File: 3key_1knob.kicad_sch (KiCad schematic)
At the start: 17 parts, among them SW1 RotaryEncoder_Switch, U4 Kailh_socket_MX, U5 Kailh_socket_MX, U6 Kailh_socket_MX

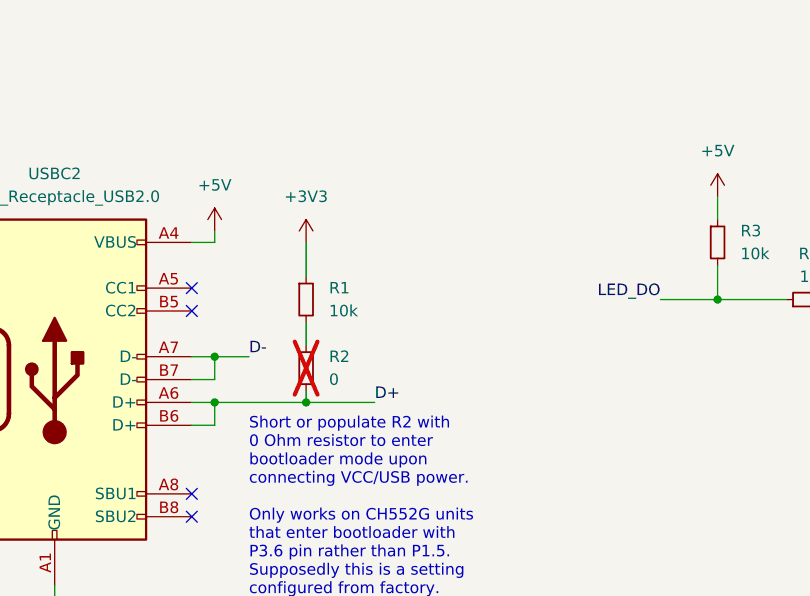
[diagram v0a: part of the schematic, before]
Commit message: Finish ground fills; Add 2 pin header; Update 3D models
This completes the PCB drawing based off the (questionable) original
design. Due to odd signal routing, there are several ground fill islands
that had to be addressed by placing microvias.

Note that with JLCPCB DRC constraints, there will be some spacing
violations due to the USBC footprint used. The USBC footprint has 2
mounting holes which are too close to power pads.

This also hides R2 resistor 3D model and displays 16-SOIC-3.9x9.9mm 3D
model. For reference, R2 is unconnected, and 16-SOP-3.9x9.9mm lacks a 3D
model so I used 16-SOIC variant instead.
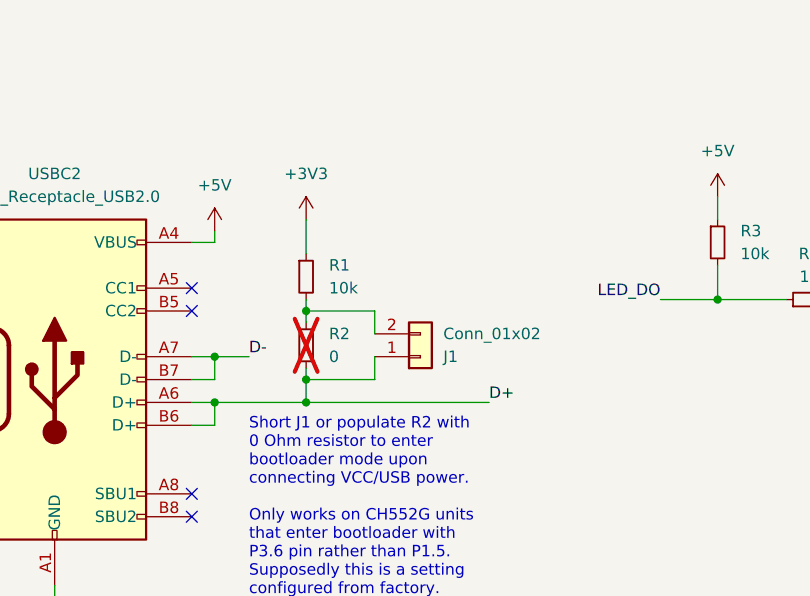
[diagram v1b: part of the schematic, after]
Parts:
- added J1: Conn_01x02, Connector_PinHeader_1.27mm:PinHeader_1x02_P1.27mm_Vertical, symbol Connector_Generic:Conn_01x02
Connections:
- net D+: now also J1.1 (Pin_1)
- net at R1.2, R2.1: now also J1.2 (Pin_2)
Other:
- note added: "Short J1 or populate R2 with 0 Ohm resistor to enter bootloader mode upon connecting VCC/USB power. Only works on CH552G units that enter bootloader with P3.6 pin rather than P1.5. Supposedly this is a setting configured from factory."
- note removed: "Short or populate R2 with 0 Ohm resistor to enter bootloader mode upon connecting VCC/USB power. Only works on CH552G units that enter bootloader with P3.6 pin rather than P1.5. Supposedly this is a setting configured from factory."
- moved on the sheet: R1, R2
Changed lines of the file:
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@@
   (junction (at 105.41 71.12) (diameter 0) (color 0 0 0 0)
+  )
+  (junction (at 59.69 80.01) (diameter 0) (color 0 0 0 0)
+  )
+  (junction (at 59.69 72.39) (diameter 0) (color 0 0 0 0)
   )
   (junction (at 49.53 82.55) (diameter 0) (color 0 0 0 0)
@@
     (stroke (width 0) (type default))
   )
+  (wire (pts (xy 59.69 80.01) (xy 59.69 82.55))
+    (stroke (width 0) (type default))
+  )
   (wire (pts (xy 46.99 82.55) (xy 49.53 82.55))
     (stroke (width 0) (type default))
@@
     (stroke (width 0) (type default))
   )
+  (wire (pts (xy 67.31 72.39) (xy 59.69 72.39))
+    (stroke (width 0) (type default))
+  )
   (wire (pts (xy 127 39.37) (xy 124.46 39.37))
     (stroke (width 0) (type default))
@@
     (stroke (width 0) (type default))
   )
+  (wire (pts (xy 67.31 80.01) (xy 59.69 80.01))
+    (stroke (width 0) (type default))
+  )
   (wire (pts (xy 49.53 77.47) (xy 53.34 77.47))
     (stroke (width 0) (type default))
@@
     (stroke (width 0) (type default))
   )
-  (wire (pts (xy 59.69 81.28) (xy 59.69 82.55))
+  (wire (pts (xy 59.69 78.74) (xy 59.69 80.01))
     (stroke (width 0) (type default))
   )
@@
     (stroke (width 0) (type default))
   )
-  (wire (pts (xy 59.69 82.55) (xy 67.31 82.55))
+  (wire (pts (xy 59.69 82.55) (xy 80.01 82.55))
     (stroke (width 0) (type default))
   )
@@
     (stroke (width 0) (type default))
   )
+  (wire (pts (xy 59.69 72.39) (xy 59.69 73.66))
+    (stroke (width 0) (type default))
+  )
+  (wire (pts (xy 67.31 77.47) (xy 67.31 80.01))
+    (stroke (width 0) (type default))
+  )
   (wire (pts (xy 49.53 85.09) (xy 49.53 82.55))
     (stroke (width 0) (type default))
@@
     (stroke (width 0) (type default))
   )
-  (wire (pts (xy 59.69 73.66) (xy 59.69 76.2))
-    (stroke (width 0) (type default))
-  )
-  (wire (pts (xy 59.69 64.77) (xy 59.69 68.58))
+  (wire (pts (xy 59.69 71.12) (xy 59.69 72.39))
+    (stroke (width 0) (type default))
+  )
+  (wire (pts (xy 59.69 62.23) (xy 59.69 66.04))
     (stroke (width 0) (type default))
   )
@@
   )
   (wire (pts (xy 128.27 147.32) (xy 133.35 147.32))
+    (stroke (width 0) (type default))
+  )
+  (wire (pts (xy 67.31 74.93) (xy 67.31 72.39))
     (stroke (width 0) (type default))
   )
@@
     (effects (font (size 1.27 1.27)) (justify left bottom))
   )
-  (text "Short or populate R2 with\n0 Ohm resistor to enter\nbootloader mode upon\nconnecting VCC/USB power.\n\nOnly works on CH552G units\nthat enter bootloader with\nP3.6 pin rather than P1.5.\nSupposedly this is a setting\nconfigured from factory."
+  (text "Short J1 or populate R2 with\n0 Ohm resistor to enter\nbootloader mode upon\nconnecting VCC/USB power.\n\nOnly works on CH552G units\nthat enter bootloader with\nP3.6 pin rather than P1.5.\nSupposedly this is a setting\nconfigured from factory."
     (at 53.34 104.14 0)
     (effects (font (size 1.27 1.27)) (justify left bottom))
@@
     (effects (font (size 1.27 1.27)) (justify left bottom))
   )
-  (label "D+" (at 67.31 82.55 0) (fields_autoplaced)
+  (label "D+" (at 80.01 82.55 0) (fields_autoplaced)
     (effects (font (size 1.27 1.27)) (justify left bottom))
   )
@@
     )
   )
-  (symbol (lib_id "Device:R_Small") (at 59.69 71.12 0) (unit 1)
-    (in_bom yes) (on_board yes) (dnp no) (fields_autoplaced)
-    (property "Reference" "R1" (at 62.23 69.85 0)
-      (effects (font (size 1.27 1.27)) (justify left))
-    )
-    (property "Value" "10k" (at 62.23 72.39 0)
-      (effects (font (size 1.27 1.27)) (justify left))
-    )
-    (property "Footprint" "Resistor_SMD:R_0603_1608Metric" (at 59.69 71.12 0)
-      (effects (font (size 1.27 1.27)) hide)
-    )
-    (property "Datasheet" "~" (at 59.69 71.12 0)
+  (symbol (lib_id "Device:R_Small") (at 59.69 68.58 0) (unit 1)
+    (in_bom yes) (on_board yes) (dnp no) (fields_autoplaced)
+    (property "Reference" "R1" (at 62.23 67.31 0)
+      (effects (font (size 1.27 1.27)) (justify left))
+    )
+    (property "Value" "10k" (at 62.23 69.85 0)
+      (effects (font (size 1.27 1.27)) (justify left))
+    )
+    (property "Footprint" "Resistor_SMD:R_0603_1608Metric" (at 59.69 68.58 0)
+      (effects (font (size 1.27 1.27)) hide)
+    )
+    (property "Datasheet" "~" (at 59.69 68.58 0)
       (effects (font (size 1.27 1.27)) hide)
     )
@@
     )
   )
-  (symbol (lib_id "power:+3V3") (at 59.69 64.77 0) (unit 1)
-    (in_bom yes) (on_board yes) (dnp no) (fields_autoplaced)
-    (property "Reference" "#PWR022" (at 59.69 68.58 0)
-      (effects (font (size 1.27 1.27)) hide)
-    )
-    (property "Value" "+3V3" (at 59.69 59.69 0)
-      (effects (font (size 1.27 1.27)))
-    )
-    (property "Footprint" "" (at 59.69 64.77 0)
-      (effects (font (size 1.27 1.27)) hide)
-    )
-    (property "Datasheet" "" (at 59.69 64.77 0)
+  (symbol (lib_id "power:+3V3") (at 59.69 62.23 0) (unit 1)
+    (in_bom yes) (on_board yes) (dnp no) (fields_autoplaced)
+    (property "Reference" "#PWR022" (at 59.69 66.04 0)
+      (effects (font (size 1.27 1.27)) hide)
+    )
+    (property "Value" "+3V3" (at 59.69 57.15 0)
+      (effects (font (size 1.27 1.27)))
+    )
+    (property "Footprint" "" (at 59.69 62.23 0)
+      (effects (font (size 1.27 1.27)) hide)
+    )
+    (property "Datasheet" "" (at 59.69 62.23 0)
       (effects (font (size 1.27 1.27)) hide)
     )
@@
     )
   )
-  (symbol (lib_id "Device:R_Small") (at 59.69 78.74 0) (unit 1)
+  (symbol (lib_id "Device:R_Small") (at 59.69 76.2 0) (unit 1)
     (in_bom yes) (on_board yes) (dnp yes) (fields_autoplaced)
-    (property "Reference" "R2" (at 62.23 77.47 0)
-      (effects (font (size 1.27 1.27)) (justify left))
-    )
-    (property "Value" "0" (at 62.23 80.01 0)
-      (effects (font (size 1.27 1.27)) (justify left))
-    )
-    (property "Footprint" "Resistor_SMD:R_0603_1608Metric" (at 59.69 78.74 0)
-      (effects (font (size 1.27 1.27)) hide)
-    )
-    (property "Datasheet" "~" (at 59.69 78.74 0)
+    (property "Reference" "R2" (at 62.23 74.93 0)
+      (effects (font (size 1.27 1.27)) (justify left))
+    )
+    (property "Value" "0" (at 62.23 77.47 0)
+      (effects (font (size 1.27 1.27)) (justify left))
+    )
+    (property "Footprint" "Resistor_SMD:R_0603_1608Metric" (at 59.69 76.2 0)
+      (effects (font (size 1.27 1.27)) hide)
+    )
+    (property "Datasheet" "~" (at 59.69 76.2 0)
       (effects (font (size 1.27 1.27)) hide)
     )
@@
         )
       )
+    )
+  )
+  (symbol (lib_id "Connector_Generic:Conn_01x02") (at 72.39 77.47 0) (mirror x) (unit 1)
+    (in_bom yes) (on_board yes) (dnp no)
+    (property "Reference" "J1" (at 74.93 77.47 0)
+      (effects (font (size 1.27 1.27)) (justify left))
+    )
+    (property "Value" "Conn_01x02" (at 74.93 74.93 0)
+      (effects (font (size 1.27 1.27)) (justify left))
+    )
+    (property "Footprint" "Connector_PinHeader_1.27mm:PinHeader_1x02_P1.27mm_Vertical" (at 72.39 77.47 0)
+      (effects (font (size 1.27 1.27)) hide)
+    )
+    (property "Datasheet" "~" (at 72.39 77.47 0)
+      (effects (font (size 1.27 1.27)) hide)
+    )
+    (pin "1")
+    (pin "2")
+    (instances
+      (project "3key_1knob"
+        (path "/9be3aa4b-ba54-4f6f-960a-567b3ba38f36"
+          (reference "J1") (unit 1)
+        )
+      )

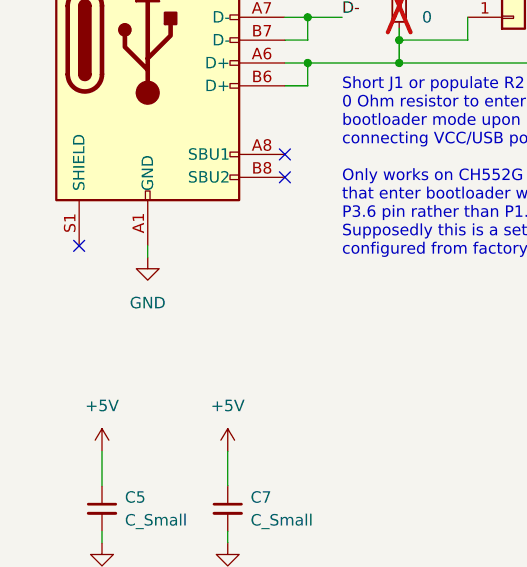
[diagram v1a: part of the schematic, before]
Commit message: Connect USBC receptacle and Rotary Encoder shield to ground; Adjust traces
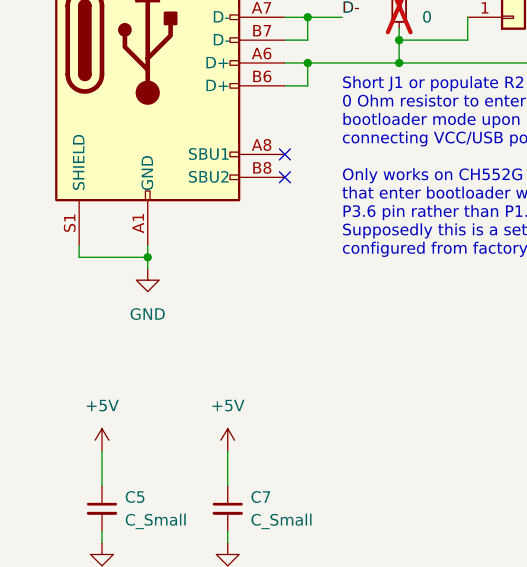
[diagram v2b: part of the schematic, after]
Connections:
- net GND: now also USBC2.S1 (SHIELD)
- no-connect marks 10 -> 9
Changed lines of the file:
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@@
   (junction (at 59.69 80.01) (diameter 0) (color 0 0 0 0)
+  )
+  (junction (at 31.75 104.14) (diameter 0) (color 0 0 0 0)
   )
   (junction (at 59.69 72.39) (diameter 0) (color 0 0 0 0)
@@
   (no_connect (at 46.99 92.71))
   (no_connect (at 46.99 69.85))
-  (no_connect (at 24.13 102.87))
   (no_connect (at 46.99 95.25))
   (no_connect (at 133.35 132.08))
@@
     (stroke (width 0) (type default))
   )
+  (wire (pts (xy 31.75 104.14) (xy 31.75 105.41))
+    (stroke (width 0) (type default))
+  )
   (wire (pts (xy 160.02 39.37) (xy 162.56 39.37))
     (stroke (width 0) (type default))
@@
     (stroke (width 0) (type default))
   )
+  (wire (pts (xy 24.13 104.14) (xy 31.75 104.14))
+    (stroke (width 0) (type default))
+  )
   (wire (pts (xy 46.99 64.77) (xy 49.53 64.77))
     (stroke (width 0) (type default))
@@
   )
   (wire (pts (xy 137.16 39.37) (xy 140.97 39.37))
+    (stroke (width 0) (type default))
+  )
+  (wire (pts (xy 24.13 102.87) (xy 24.13 104.14))
     (stroke (width 0) (type default))
   )
@@
     )
   )
-  (symbol (lib_id "power:GND") (at 31.75 104.14 0) (unit 1)
-    (in_bom yes) (on_board yes) (dnp no) (fields_autoplaced)
-    (property "Reference" "#PWR010" (at 31.75 110.49 0)
-      (effects (font (size 1.27 1.27)) hide)
-    )
-    (property "Value" "GND" (at 31.75 109.22 0)
-      (effects (font (size 1.27 1.27)))
-    )
-    (property "Footprint" "" (at 31.75 104.14 0)
-      (effects (font (size 1.27 1.27)) hide)
-    )
-    (property "Datasheet" "" (at 31.75 104.14 0)
-      (effects (font (size 1.27 1.27)) hide)
-    )
+  (symbol (lib_id "power:GND") (at 31.75 105.41 0) (unit 1)
+    (in_bom yes) (on_board yes) (dnp no) (fields_autoplaced)
+    (property "Reference" "#PWR010" (at 31.75 111.76 0)
+      (effects (font (size 1.27 1.27)) hide)
+    )
+    (property "Value" "GND" (at 31.75 110.49 0)
+      (effects (font (size 1.27 1.27)))
+    )
+    (property "Footprint" "" (at 31.75 105.41 0)
+      (effects (font (size 1.27 1.27)) hide)
+    )
+    (property "Datasheet" "" (at 31.75 105.41 0)
+      (effects (font (size 1.27 1.27)) hide)
+    )

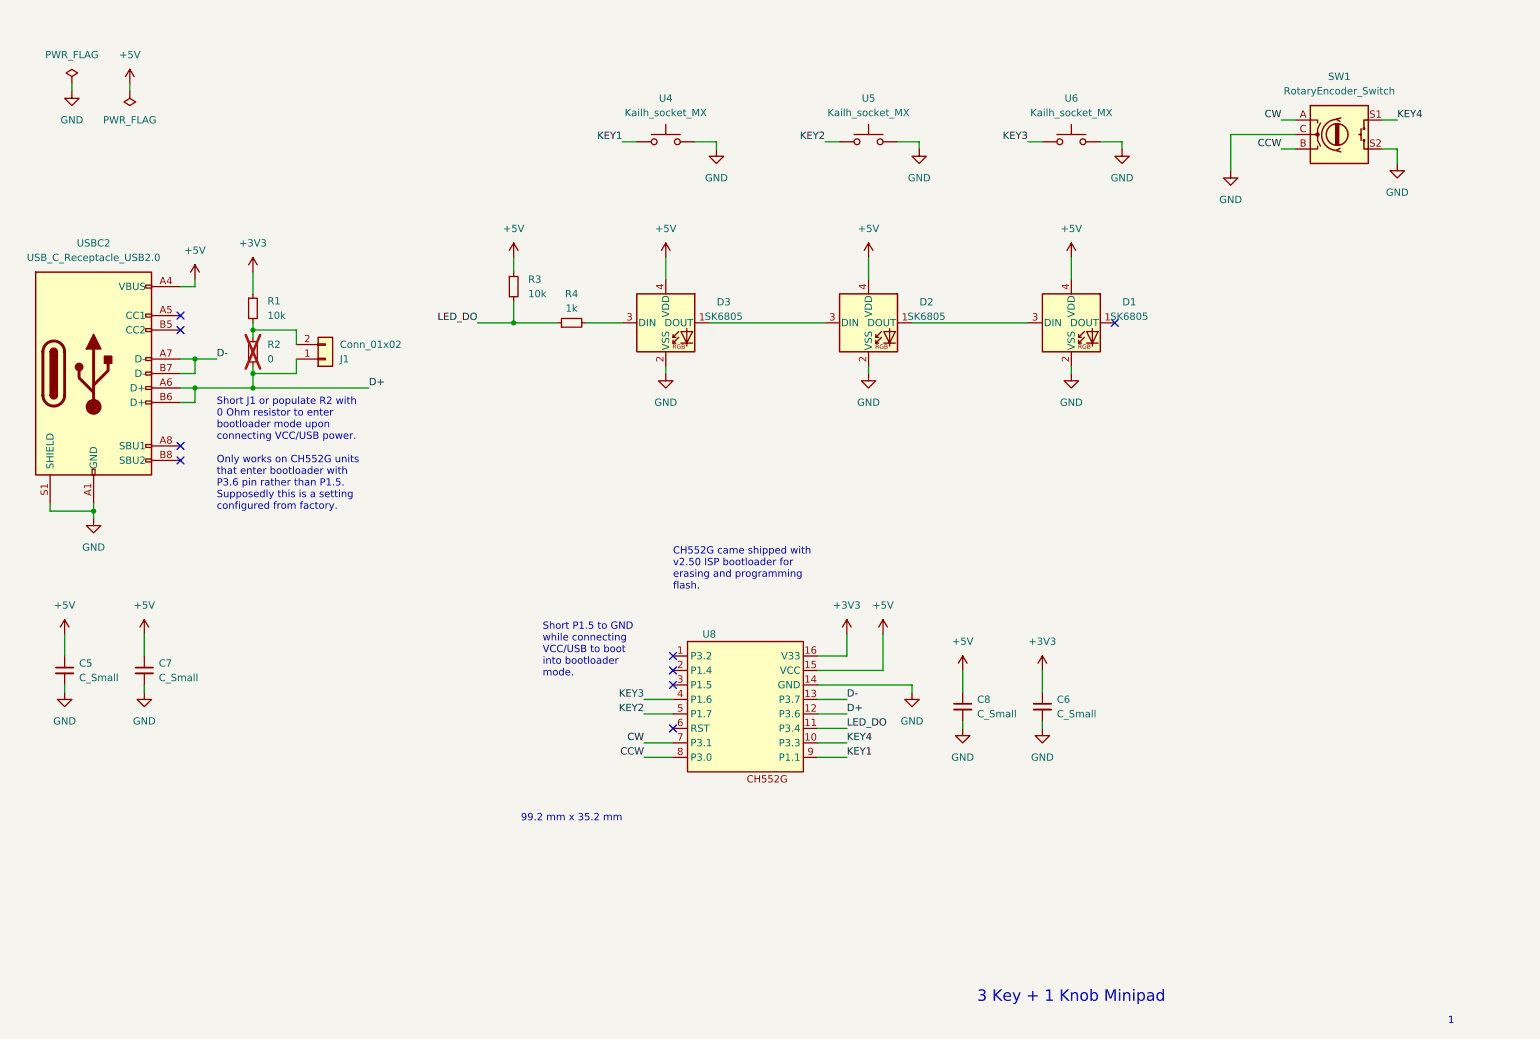
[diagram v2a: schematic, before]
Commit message: Convert signal nets to global nets; Update sch description; Minor PCB trace update
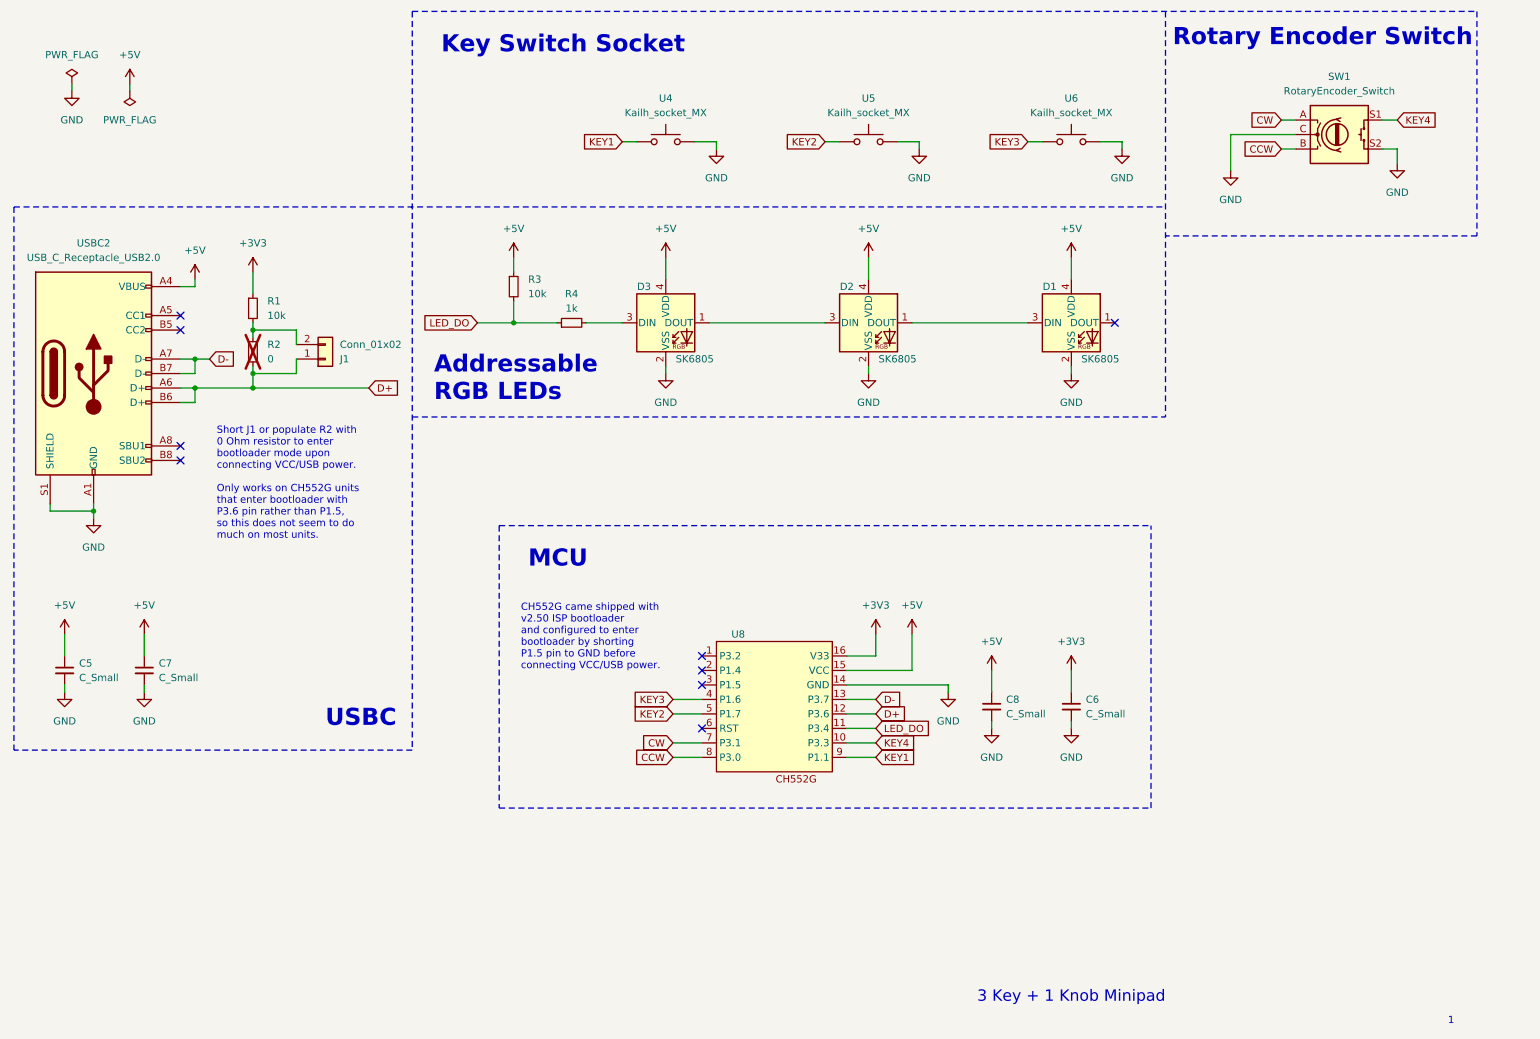
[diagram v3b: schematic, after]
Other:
- note added: "Addressable RGB LEDs"
- note added: "CH552G came shipped with v2.50 ISP bootloader and configured to enter bootloader by shorting P1.5 pin to GND before connecting VCC/USB power."
- note added: "Key Switch Socket"
- note added: "MCU"
- note added: "Rotary Encoder Switch"
- note added: "Short J1 or populate R2 with 0 Ohm resistor to enter bootloader mode upon connecting VCC/USB power. Only works on CH552G units that enter bootloader with P3.6 pin rather than P1.5, so this does not seem to do much on most units."
- note added: "USBC"
- note removed: "99.2 mm x 35.2 mm"
- note removed: "CH552G came shipped with v2.50 ISP bootloader for erasing and programming flash."
- note removed: "Short J1 or populate R2 with 0 Ohm resistor to enter bootloader mode upon connecting VCC/USB power. Only works on CH552G units that enter bootloader with P3.6 pin rather than P1.5. Supposedly this is a setting configured from factory."
- note removed: "Short P1.5 to GND while connecting VCC/USB to boot into bootloader mode."
- moved on the sheet: C6, C8, U8
